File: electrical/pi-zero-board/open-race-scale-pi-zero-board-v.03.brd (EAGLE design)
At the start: 96.5 x 45.4 mm, 68 parts, among them J5 PIN20X2, Q1 MMBT4403, Q2 MMBT4403, Q3 MMBT4403, Q4 MMBT4403, U1 HX711, U2 HX711, U3 HX711, U4 HX711

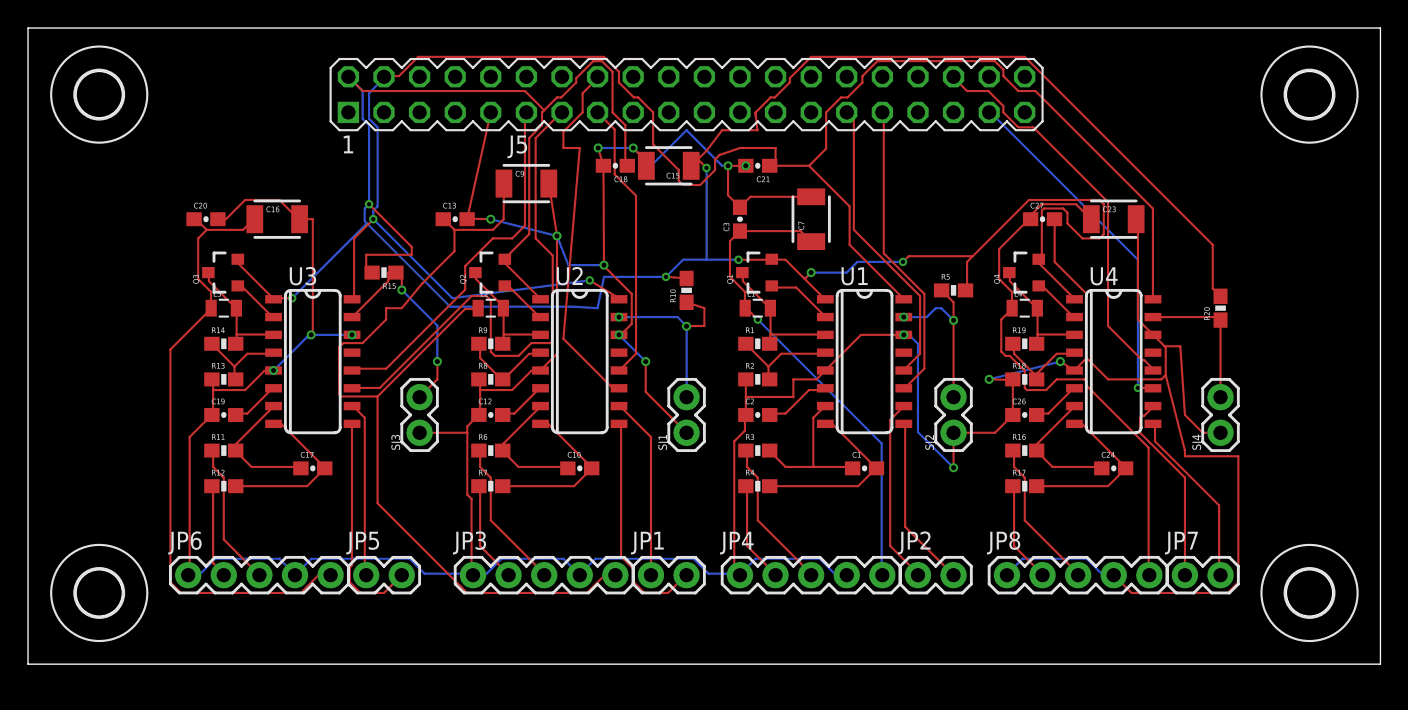
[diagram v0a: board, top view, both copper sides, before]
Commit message: silk screen
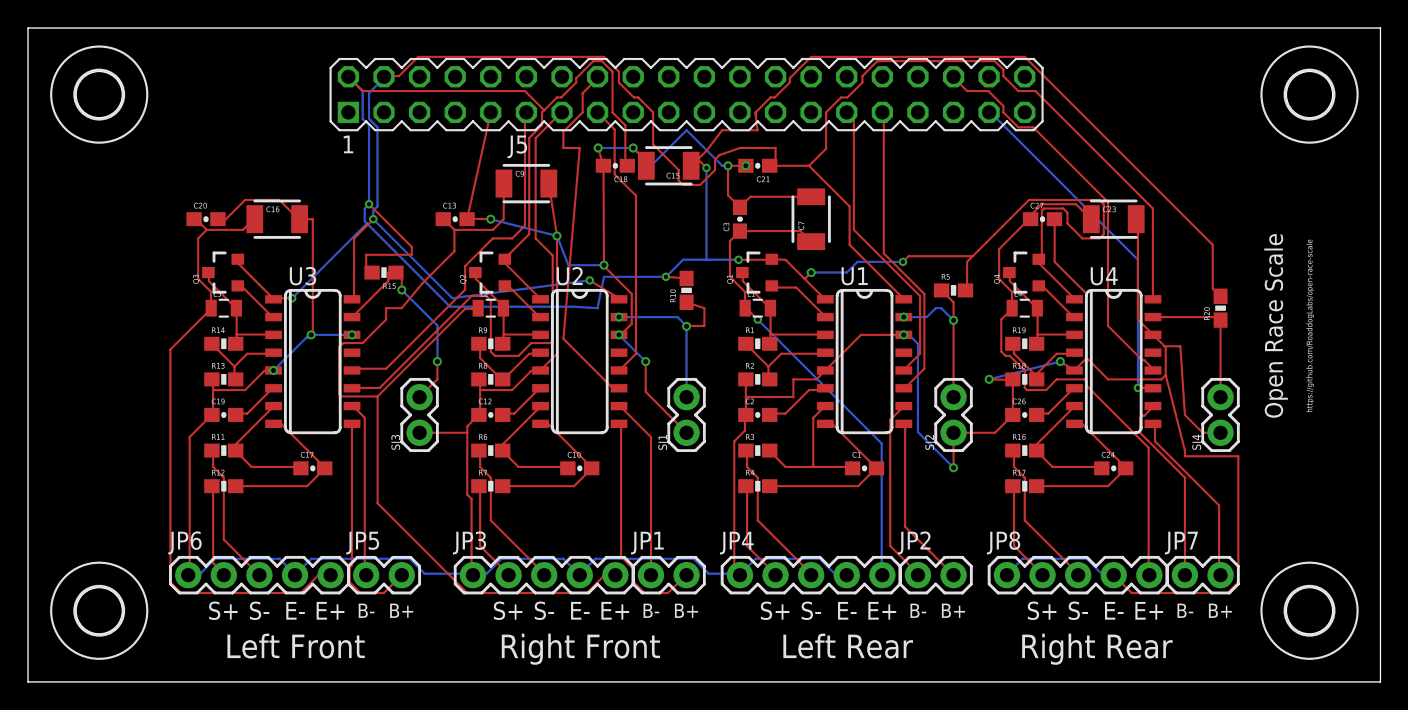
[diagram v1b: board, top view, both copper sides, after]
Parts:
- moved H1 1.27 mm to (-1.27, 44.5)
- moved H4 1.27 mm to (85.1, 44.5)
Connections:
- net N$11 renamed B+1
- net N$12 renamed B-1
- net N$13 renamed B-4
- net N$14 renamed B+2
- net N$15 renamed B-2
- net N$8 renamed B+4
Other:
- board size 96.5 x 45.4 mm -> 96.5 x 46.7 mm
- board text added: "B+"
- board text added: "B-"
- board text added: "E+"
- board text added: "E-"
- board text added: "Left Front"
- board text added: "Left Rear"
- board text added: "Open Race Scale"
- board text added: "Right Front"
- board text added: "Right Rear"
- board text added: "S+"
- board text added: "S-"
- board text added: "https://github.com/RoaddogLabs/open-race-scale"
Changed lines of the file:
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@@
 <setting verticaltext="up"/>
 </settings>
-<grid distance="50" unitdist="mil" unit="mil" style="lines" multiple="1" display="no" altdistance="5" altunitdist="mil" altunit="mil"/>
+<grid distance="50" unitdist="mil" unit="mil" style="lines" multiple="1" display="yes" altdistance="5" altunitdist="mil" altunit="mil"/>
 <layers>
 <layer number="1" name="Top" color="4" fill="1" visible="yes" active="yes"/>
@@
 <board>
 <plain>
-<wire x1="-6.35" y1="40.64" x2="90.15" y2="40.64" width="0" layer="20"/>
-<wire x1="90.15" y1="40.64" x2="90.15" y2="86.03" width="0" layer="20"/>
+<wire x1="-6.35" y1="39.37" x2="90.15" y2="39.37" width="0" layer="20"/>
+<wire x1="90.15" y1="39.37" x2="90.15" y2="86.03" width="0" layer="20"/>
 <wire x1="90.15" y1="86.03" x2="-6.35" y2="86.03" width="0" layer="20"/>
-<wire x1="-6.35" y1="86.03" x2="-6.35" y2="40.64" width="0" layer="20"/>
+<wire x1="-6.35" y1="86.03" x2="-6.35" y2="39.37" width="0" layer="20"/>
+<text x="7.62" y="44.45" size="1.27" layer="21" align="center">S+</text>
+<text x="10.16" y="44.45" size="1.27" layer="21" align="center">S-</text>
+<text x="12.7" y="44.45" size="1.27" layer="21" align="center">E-</text>
+<text x="15.24" y="44.45" size="1.27" layer="21" align="center">E+</text>
+<text x="17.78" y="44.45" size="1.016" layer="21" align="center">B-</text>
+<text x="20.32" y="44.45" size="1.016" layer="21" align="center">B+</text>
+<text x="82.55" y="64.77" size="1.27" layer="21" rot="R90" align="center">Open Race Scale</text>
+<text x="85.09" y="64.77" size="0.4064" layer="21" rot="R90" align="center">https://github.com/RoaddogLabs/open-race-scale</text>
+<text x="27.94" y="44.45" size="1.27" layer="21" align="center">S+</text>
+<text x="30.48" y="44.45" size="1.27" layer="21" align="center">S-</text>
+<text x="33.02" y="44.45" size="1.27" layer="21" align="center">E-</text>
+<text x="38.1" y="44.45" size="1.016" layer="21" align="center">B-</text>
+<text x="35.56" y="44.45" size="1.27" layer="21" align="center">E+</text>
+<text x="40.64" y="44.45" size="1.016" layer="21" align="center">B+</text>
+<text x="12.7" y="41.91" size="1.6764" layer="21" align="center">Left Front</text>
+<text x="33.02" y="41.91" size="1.6764" layer="21" align="center">Right Front</text>
+<text x="52.07" y="41.91" size="1.6764" layer="21" align="center">Left Rear</text>
+<text x="69.85" y="41.91" size="1.6764" layer="21" align="center">Right Rear</text>
+<text x="46.99" y="44.45" size="1.27" layer="21" align="center">S+</text>
+<text x="49.53" y="44.45" size="1.27" layer="21" align="center">S-</text>
+<text x="52.07" y="44.45" size="1.27" layer="21" align="center">E-</text>
+<text x="54.61" y="44.45" size="1.27" layer="21" align="center">E+</text>
+<text x="57.15" y="44.45" size="1.016" layer="21" align="center">B-</text>
+<text x="59.69" y="44.45" size="1.016" layer="21" align="center">B+</text>
+<text x="66.04" y="44.45" size="1.27" layer="21" align="center">S+</text>
+<text x="68.58" y="44.45" size="1.27" layer="21" align="center">S-</text>
+<text x="71.12" y="44.45" size="1.27" layer="21" align="center">E-</text>
+<text x="73.66" y="44.45" size="1.27" layer="21" align="center">E+</text>
+<text x="76.2" y="44.45" size="1.016" layer="21" align="center">B-</text>
+<text x="78.74" y="44.45" size="1.016" layer="21" align="center">B+</text>
 </plain>
 <attributes>
@@
 <attribute name="PROD_ID" value="IC-12445" x="71.12" y="62.23" size="1.778" layer="27" rot="R270" display="off"/>
 </element>
-<element name="H1" library="holes" package="3,3" value="MOUNT-HOLE3.3" x="-1.27" y="45.72"/>
+<element name="H1" library="holes" package="3,3" value="MOUNT-HOLE3.3" x="-1.27" y="44.45"/>
 <element name="H2" library="holes" package="3,3" value="MOUNT-HOLE3.3" x="-1.27" y="81.28"/>
 <element name="H3" library="holes" package="3,3" value="MOUNT-HOLE3.3" x="85.09" y="81.28"/>
-<element name="H4" library="holes" package="3,3" value="MOUNT-HOLE3.3" x="85.09" y="45.72"/>
+<element name="H4" library="holes" package="3,3" value="MOUNT-HOLE3.3" x="85.09" y="44.45"/>
 </elements>
 <signals>
@@
 <wire x1="63.8556" y1="65.9892" x2="63.87" y2="66.04" width="0.1524" layer="1"/>
 </signal>
-<signal name="N$8">
+<signal name="B+4">
 <contactref element="U4" pad="10"/>
 <contactref element="JP7" pad="1"/>
@@
 <wire x1="73.914" y1="58.9788" x2="73.92" y2="59.055" width="0.1524" layer="1"/>
 </signal>
-<signal name="N$11">
+<signal name="B+1">
 <contactref element="U3" pad="10"/>
 <contactref element="JP5" pad="1"/>
@@
 <wire x1="17.6784" y1="47.0916" x2="17.78" y2="46.99" width="0.1524" layer="1"/>
 </signal>
-<signal name="N$12">
+<signal name="B-1">
 <contactref element="JP5" pad="2"/>
 <contactref element="U3" pad="9"/>
@@
 <wire x1="16.764" y1="57.7596" x2="16.77" y2="57.785" width="0.1524" layer="1"/>
 </signal>
-<signal name="N$13">
+<signal name="B-4">
 <contactref element="JP7" pad="2"/>
 <contactref element="U4" pad="9"/>
@@
 <wire x1="78.6384" y1="47.0916" x2="78.74" y2="46.99" width="0.1524" layer="1"/>
 </signal>
-<signal name="N$14">
+<signal name="B+2">
 <contactref element="JP1" pad="1"/>
 <contactref element="U2" pad="10"/>
@@
 <wire x1="35.9664" y1="58.9788" x2="35.82" y2="59.055" width="0.1524" layer="1"/>
 </signal>
-<signal name="N$15">
+<signal name="B-2">
 <contactref element="JP1" pad="2"/>
 <contactref element="U2" pad="9"/>
